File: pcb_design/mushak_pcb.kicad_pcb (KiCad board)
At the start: 2 copper layers, 57.7 x 40 mm, 115 parts, among them IC1 AS5600-ASOT, IC2 AS5600-ASOT, J1 Conn_01x04_Male, J10 IR_1, J11 AS5600_1, J12 IR_2, J13 AS5600_2, J14 IR_3, J15 ToF, J16 IR_4, J17 ToF, J2 Conn_01x02_Female, J3 BLE_Conn, J4 AS5600_Left, J5 AS5600_Right, J6 IR_1, J7 IR_3, J8 IR_2, J9 IR_4, M1 motor, M2 motor, Q1 DMN3065LW-7, Q2 DMN3065LW-7, Q3 DMN3065LW-7, Q4 DMN3065LW-7, Q5 DMN3065LW-7, SW1 SW_Push, SW2 SW_Push, U1 BA30BC0FP-E2, U3 DRV8833PW, U4 VL6180XV0NR/1, U5 MPU-6500, U6 STM32F405RGTx, Y1 25Mhz, Y2 32.769kHz

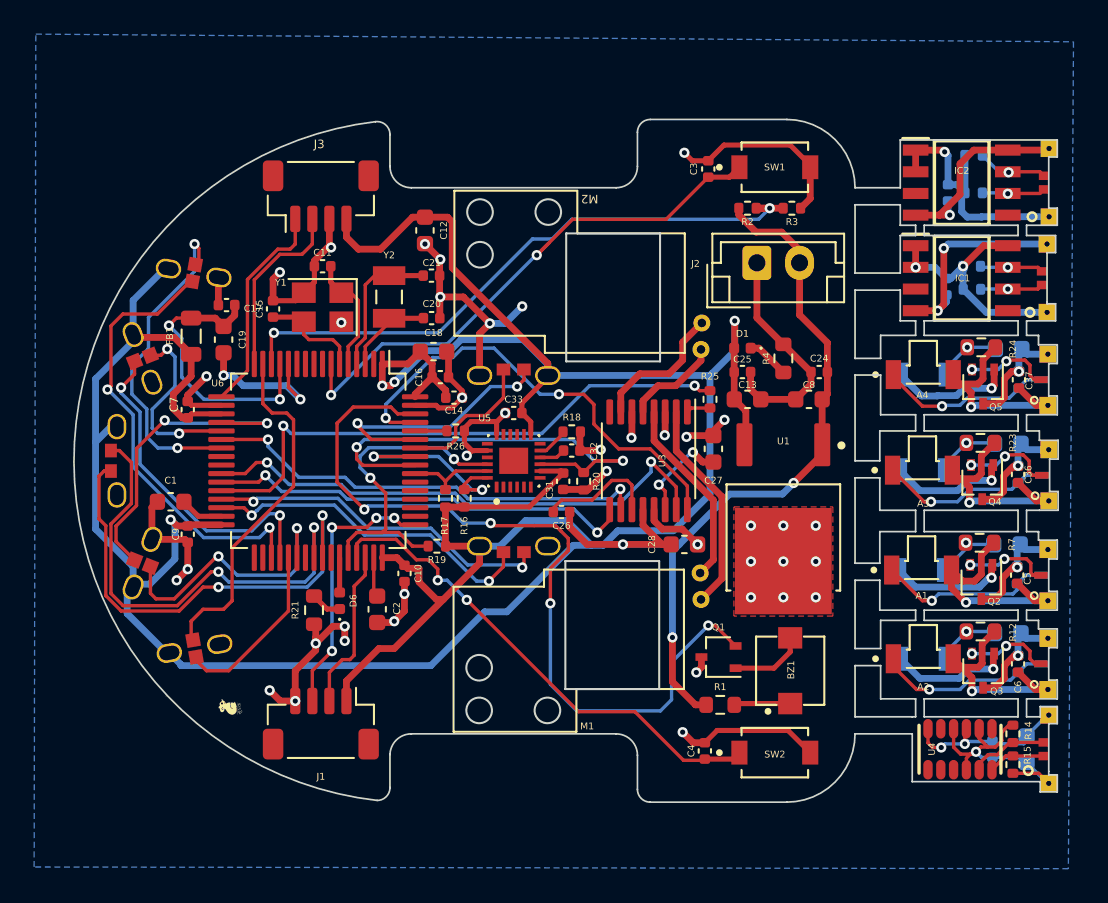
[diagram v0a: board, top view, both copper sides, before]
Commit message: add graphiccs on PCB
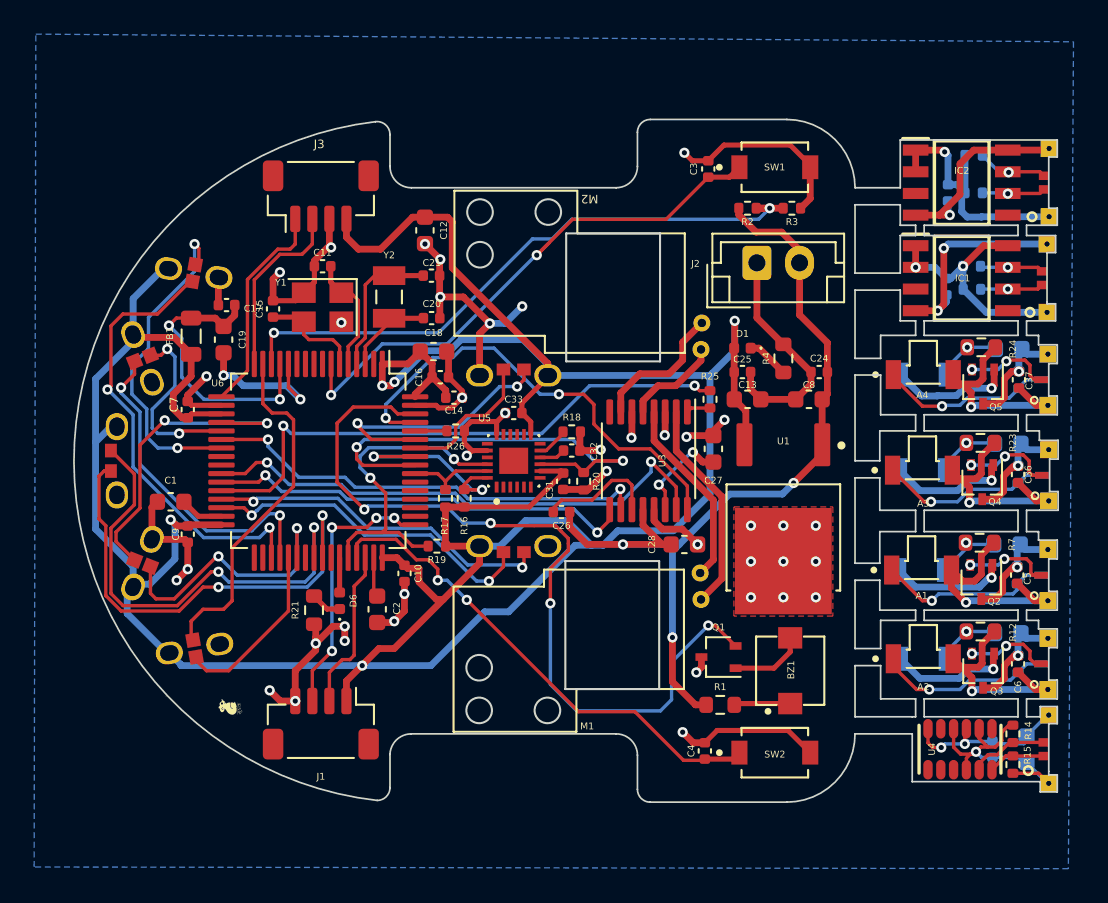
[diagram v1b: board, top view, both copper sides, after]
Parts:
- added G***: LOGO, mushak_mount_footprint:euro, B.Cu at (161.4, 84.9)
- added G***: LOGO, mushak_mount_footprint:vjti_logo, B.Cu at (163.1, 108.0)
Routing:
- net +3V0: track 196.8 -> 196.4 mm, vias 4 -> 5

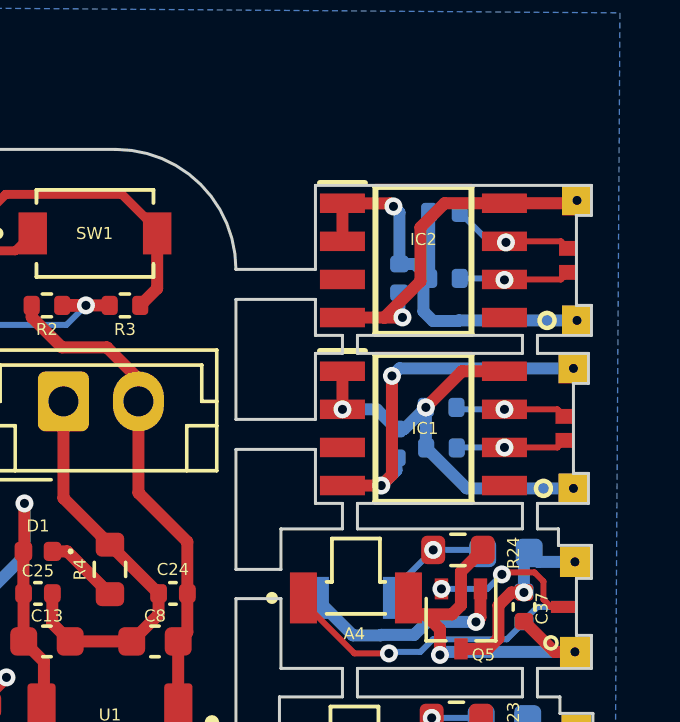
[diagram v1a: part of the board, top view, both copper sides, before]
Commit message: changed AS5600 to AS5048B
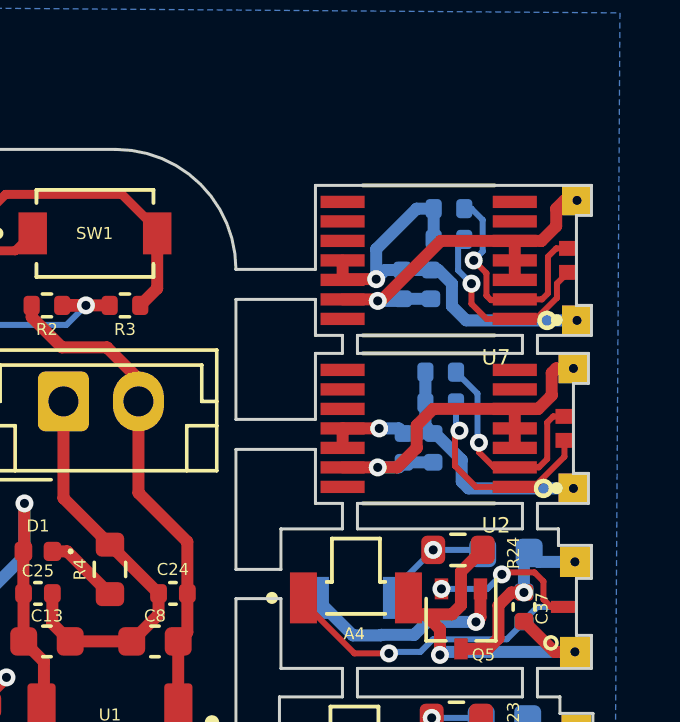
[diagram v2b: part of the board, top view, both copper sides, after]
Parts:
- removed the G*** at (161.4, 84.9)
- removed IC1, IC2: AS5600-ASOT, AS5600-ASOT:SOIC127P600X175-8N
- added C40: 0.1uF, Capacitor_SMD:C_0402_1005Metric, B.Cu at (200.6, 87.0)
- added C41: 0.1uF, Capacitor_SMD:C_0402_1005Metric, B.Cu at (200.5, 81.5)
- added U2: AS5048B-HTSP, AS5048B-HTSP:SOP65P640X120-14N, F.Cu at (200.4, 86.3)
- added U7: AS5048B-HTSP, AS5048B-HTSP:SOP65P640X120-14N, F.Cu at (200.4, 80.7)
- moved R5 2.53 mm to (200.8, 84.4)
- moved R10 2.33 mm to (201.1, 79.0)
- moved R9 0.91 mm to (201.1, 80.0)
- moved C23 0.29 mm to (199.6, 87.0)
- moved C22 0.22 mm to (199.6, 81.5)
- moved R8 0.15 mm to (200.8, 85.5)
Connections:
- R10 pad 2: /AS5600_Right/SDA_s -> /AS5600_Right/SCL_s
- R5 pad 2: /AS5600_Left/SDA_s -> /AS5600_Left/SCL_s
- R8 pad 2: /AS5600_Left/SCL_s -> /AS5600_Left/SDA_s
- R9 pad 2: /AS5600_Right/SCL_s -> /AS5600_Right/SDA_s
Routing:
- net /AS5600_Left/SCL_s: track 3.72 -> 7.46 mm
- net /AS5600_Right/SCL_s: track 4.24 -> 7.81 mm
- net /AS5600_Left/SDA_s: track 3.69 -> 7.11 mm
- net /AS5600_Right/SDA_s: track 3.74 -> 6.77 mm
- net /AS5600_Left/+3V0_s: track 14.6 -> 11.8 mm, vias 2 -> 1
- net /AS5600_Left/GND_s: track 12.4 -> 13.2 mm, vias 2 -> 1
- net /AS5600_Right/GND_s: track 12.0 -> 12.7 mm
- net /AS5600_Right/+3V0_s: track 14.8 -> 14.2 mm
